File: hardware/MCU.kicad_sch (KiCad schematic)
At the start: 34 parts, among them J2 USB_C_Receptacle_USB2.0_16P, SW1 SW_RST, SW2 SW_BOOT, U1 ESP32-WROOM-32E, U3 CP2102N-Axx-xQFN28, U4 USBLC6-2SC6

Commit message: Board resize in progress
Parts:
- C12: renamed from C_vdd1; Function (none) -> C_vdd1
- C13: renamed from C_vdd2; Function (none) -> C_vdd2
- C14: renamed from C_reg1; Function (none) -> C_reg1
- C15: renamed from C_en1; Function (none) -> C_en1
- C16: renamed from C_esp1; Function (none) -> C_esp1
- C17: renamed from C_esp2; Function (none) -> C_esp2
- C18: renamed from C_esp3; Function (none) -> C_esp3
- D3: renamed from D_led1; Function (none) -> D_led1
- J2: Function (none) -> J2
- J3: renamed from J_sens1; Function (none) -> J_sens1
- J4: renamed from J_display1; Function (none) -> J_display1
- Q2: renamed from Q_boot1; Function (none) -> Q_boot1
- Q3: renamed from Q_rst1; Function (none) -> Q_rst1
- R10: renamed from R_cc2; Function (none) -> R_cc2
- R11: renamed from R_cc1; Function (none) -> R_cc1
- R12: renamed from R_en1; Function (none) -> R_en1
- R13: renamed from R_io0; Function (none) -> R_io0
- R14: renamed from R_pu_sda1; Function (none) -> R_pu_sda1
- R15: renamed from R_pu_scl1; Function (none) -> R_pu_scl1
- R16: renamed from R_s_scl1; Function (none) -> R_s_scl1
- R17: renamed from R_s_sda1; Function (none) -> R_s_sda1
- R18: renamed from R_led1; Function (none) -> R_led1
- R7: renamed from R_vbus_top1; Function (none) -> R_vbus_top1
- R8: renamed from R_vbus_bot1; Function (none) -> R_vbus_bot1
- R9: renamed from R_rst1; Function (none) -> R_rst1
- SW1: Function (none) -> SW1
- SW2: Function (none) -> SW2
- TP4: Function (none) -> TP4
- TP5: renamed from TP7; Function (none) -> TP7
- TP6: renamed from TP5; Function (none) -> TP5
- TP7: renamed from TP6; Function (none) -> TP6
- U2: renamed from U3; Function (none) -> U3
- U3: renamed from U4; Function (none) -> U4
- U4: renamed from U1; Function (none) -> U1
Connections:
- net USB_DM: now also U3.6 (I/O1); no longer U3.4 (I/O2)
- net USB_DP: now also U3.4 (I/O2); no longer U3.6 (I/O1)
- net at J2.A6 (D+), J2.B6 (D+): now also U3.3 (I/O2); no longer U3.1 (I/O1)
- net at J2.A7 (D-), J2.B7 (D-): now also U3.1 (I/O1); no longer U3.3 (I/O2)

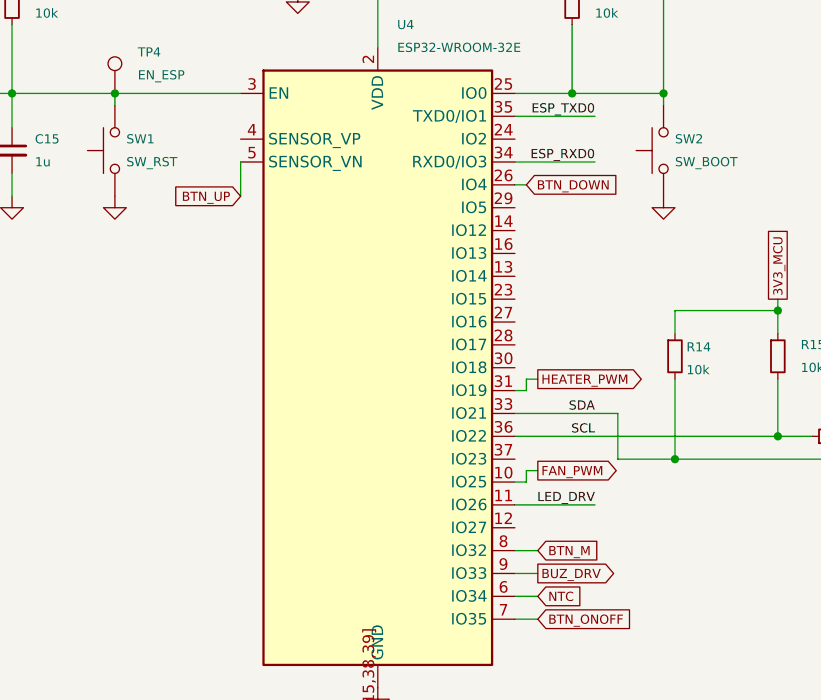
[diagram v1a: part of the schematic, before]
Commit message: Update README: GPIO map (fan/up/down pins), button description, board size under revision
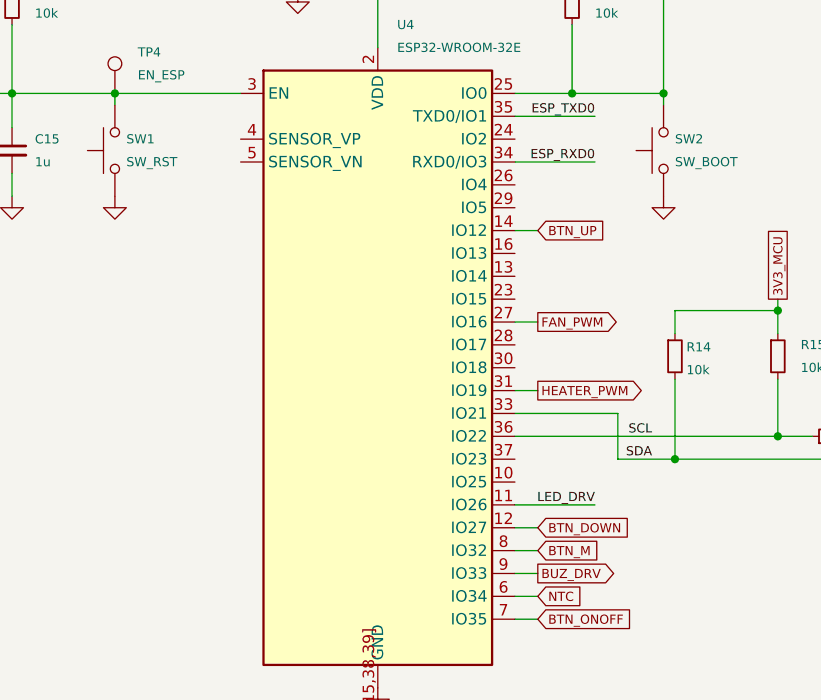
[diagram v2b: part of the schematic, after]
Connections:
- net BTN_DOWN: now also U4.12 (IO27); no longer U4.26 (IO4)
- net BTN_UP: now also U4.14 (IO12); no longer U4.5 (SENSOR_VN)
- net FAN_PWM: now also U4.27 (IO16); no longer U4.10 (IO25)
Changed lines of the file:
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@@
-	(wire
-		(pts
-			(xy 200.66 93.98) (xy 201.93 93.98)
-		)
-		(stroke
-			(width 0)
-			(type default)
-		)
-	)
 	(wire
 		(pts
@@
 	(wire
 		(pts
+			(xy 199.39 77.47) (xy 201.93 77.47)
+		)
+		(stroke
+			(width 0)
+			(type default)
+		)
+	)
+	(wire
+		(pts
 			(xy 102.87 161.29) (xy 102.87 148.59)
 		)
@@
 	(wire
 		(pts
-			(xy 200.66 104.14) (xy 201.93 104.14)
-		)
-		(stroke
-			(width 0)
-			(type default)
-		)
-	)
-	(wire
-		(pts
 			(xy 80.01 45.72) (xy 90.17 45.72)
 		)
@@
 	(wire
 		(pts
-			(xy 200.66 105.41) (xy 199.39 105.41)
-		)
-		(stroke
-			(width 0)
-			(type default)
-		)
-	)
-	(wire
-		(pts
 			(xy 119.38 54.61) (xy 119.38 68.58)
 		)
@@
 	(wire
 		(pts
+			(xy 199.39 87.63) (xy 201.93 87.63)
+		)
+		(stroke
+			(width 0)
+			(type default)
+		)
+	)
+	(wire
+		(pts
 			(xy 111.76 49.53) (xy 111.76 76.2)
 		)
@@
 	(wire
 		(pts
-			(xy 200.66 93.98) (xy 200.66 95.25)
-		)
-		(stroke
-			(width 0)
-			(type default)
-		)
-	)
-	(wire
-		(pts
 			(xy 80.01 53.34) (xy 90.17 53.34)
 		)
@@
 	(wire
 		(pts
-			(xy 168.91 73.66) (xy 168.91 69.85)
-		)
-		(stroke
-			(width 0)
-			(type default)
-		)
-	)
-	(wire
-		(pts
-			(xy 200.66 72.39) (xy 199.39 72.39)
-		)
-		(stroke
-			(width 0)
-			(type default)
-		)
-	)
-	(wire
-		(pts
 			(xy 251.46 119.38) (xy 248.92 119.38)
 		)
@@
 	(wire
 		(pts
-			(xy 200.66 104.14) (xy 200.66 105.41)
-		)
-		(stroke
-			(width 0)
-			(type default)
-		)
-	)
-	(wire
-		(pts
 			(xy 90.17 43.18) (xy 90.17 45.72)
 		)
@@
 	(wire
 		(pts
-			(xy 200.66 95.25) (xy 199.39 95.25)
+			(xy 199.39 95.25) (xy 201.93 95.25)
 		)
 		(stroke
@@
 		(pts
 			(xy 143.51 71.12) (xy 143.51 73.66)
+		)
+		(stroke
+			(width 0)
+			(type default)
+		)
+	)
+	(wire
+		(pts
+			(xy 199.39 110.49) (xy 201.93 110.49)
 		)
 		(stroke
@@
 	)
 	(label "SCL"
-		(at 208.28 100.33 180)
+		(at 214.63 100.33 180)
 		(effects
 			(font
@@
 	)
 	(label "SDA"
-		(at 208.28 97.79 180)
+		(at 214.63 102.87 180)
 		(effects
 			(font
@@
 	(global_label "BTN_DOWN"
 		(shape input)
-		(at 200.66 72.39 0)
+		(at 201.93 110.49 0)
 		(fields_autoplaced yes)
 		(effects
@@
 		)
 		(property "Intersheetrefs" "${INTERSHEET_REFS}"
-			(at 210.9824 72.39 0)
+			(at 212.2524 110.49 0)
 			(hide yes)
 			(show_name no)
@@
 	(global_label "FAN_PWM"
 		(shape output)
-		(at 201.93 104.14 0)
+		(at 201.93 87.63 0)
 		(fields_autoplaced yes)
 		(effects
@@
 		)
 		(property "Intersheetrefs" "${INTERSHEET_REFS}"
-			(at 211.2364 104.14 0)
+			(at 211.2364 87.63 0)
 			(hide yes)
 			(show_name no)
@@
 	(global_label "HEATER_PWM"
 		(shape output)
-		(at 201.93 93.98 0)
+		(at 201.93 95.25 0)
 		(fields_autoplaced yes)
 		(effects
@@
 		)
 		(property "Intersheetrefs" "${INTERSHEET_REFS}"
-			(at 213.994 93.98 0)
+			(at 213.994 95.25 0)
 			(hide yes)
 			(show_name no)
@@
 	(global_label "BTN_UP"
 		(shape input)
-		(at 168.91 73.66 180)
+		(at 201.93 77.47 0)
 		(fields_autoplaced yes)
 		(effects
@@
 				(size 1.016 1.016)
 			)
-			(justify right)
+			(justify left)
 		)
 		(property "Intersheetrefs" "${INTERSHEET_REFS}"
-			(at 160.8131 73.66 0)
+			(at 210.0269 77.47 0)
 			(hide yes)
 			(show_name no)
@@
 					(size 1.016 1.016)
 				)
-				(justify right)
-			)
-		)
+				(justify left)
+			)
+		)

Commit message: Board resize in progress
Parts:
- U2: footprint Package_DFN_QFN:QFN-28-1EP_5x5mm_P0.5mm_EP3.35x3.35mm -> FilamentDryer:CP2102N_GQFN28_5x5mm_P0.5mm_EP3.35x3.35mm
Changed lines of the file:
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@@
 			)
 		)
-		(property "Footprint" "Package_DFN_QFN:QFN-28-1EP_5x5mm_P0.5mm_EP3.35x3.35mm"
+		(property "Footprint" "FilamentDryer:CP2102N_GQFN28_5x5mm_P0.5mm_EP3.35x3.35mm"
 			(at 106.68 123.19 0)
 			(hide yes)
